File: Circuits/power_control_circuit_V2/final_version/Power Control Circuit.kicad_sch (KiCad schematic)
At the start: 35 parts, among them Q10 IRF1405, Q12 IRF1405, Q23 S8050, Q24 S8550, Q3 S8050, Q4 IRF1405, Q4 S8550, Q8 IRF1405, Q9 IRF1405, U1 PC817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

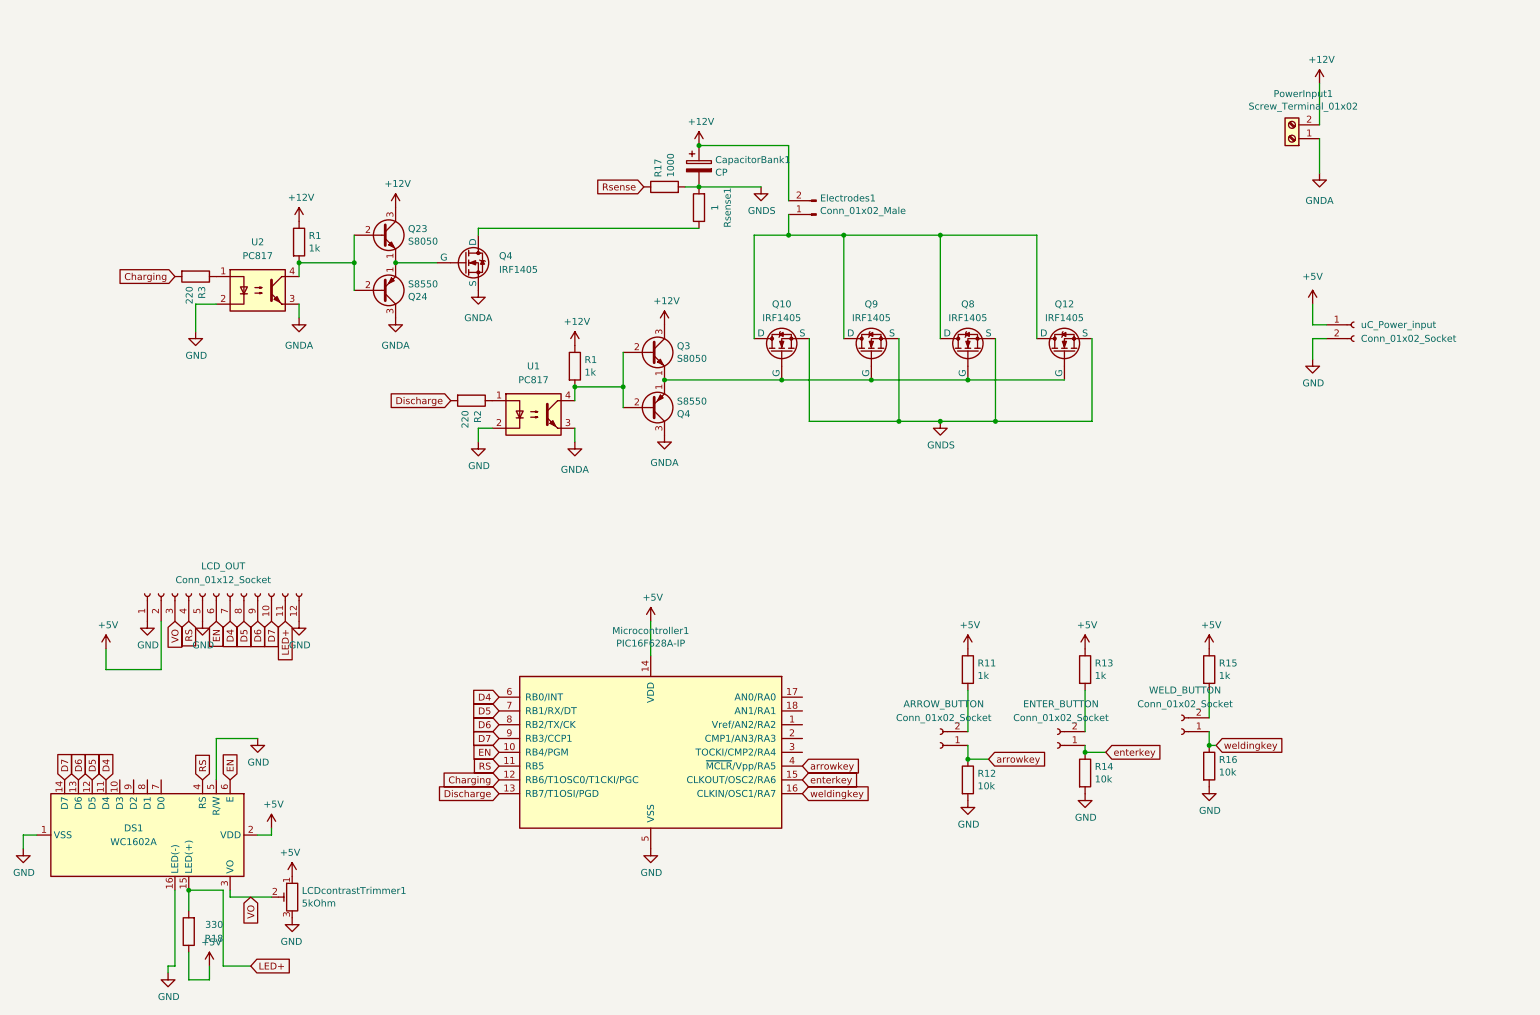
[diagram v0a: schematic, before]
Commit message: finished PCB solution, starting PCB final version|
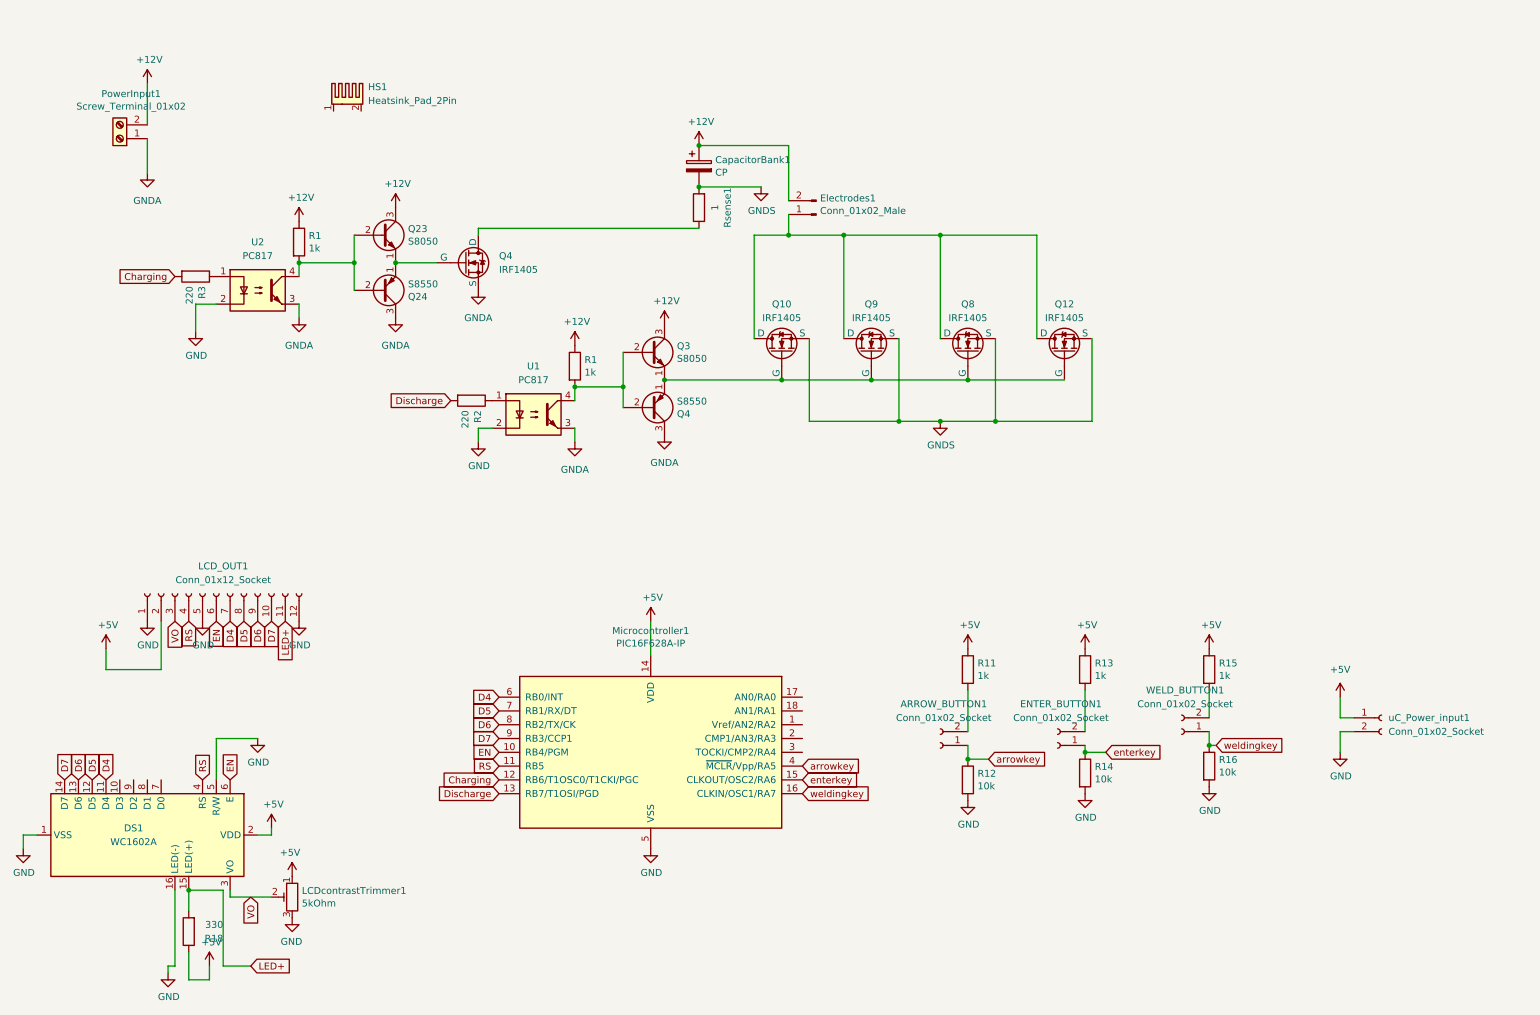
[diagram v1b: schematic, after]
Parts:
- removed R17: 1000, Resistor_THT:R_Axial_DIN0207_L6.3mm_D2.5mm_P7.62mm_Horizontal, symbol Device:R
- added HS1: Heatsink_Pad_2Pin, symbol Mechanical:Heatsink_Pad_2Pin
- ARROW_BUTTON1: renamed from ARROW_BUTTON; footprint (none) -> Connector_JST:JST_EH_B2B-EH-A_1x02_P2.50mm_Vertical
- ENTER_BUTTON1: renamed from ENTER_BUTTON; footprint (none) -> Connector_JST:JST_EH_B2B-EH-A_1x02_P2.50mm_Vertical
- LCDcontrastTrimmer1: footprint trimmer:trimmerEVND8A -> Potentiometer_THT:Potentiometer_Bourns_3386C_Horizontal
- WELD_BUTTON1: renamed from WELD_BUTTON; footprint (none) -> Connector_JST:JST_EH_B2B-EH-A_1x02_P2.50mm_Vertical
- renumbered LCD_OUT to LCD_OUT1, uC_Power_input to uC_Power_input1
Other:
- moved on the sheet: PowerInput1, uC_Power_input1

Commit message: finished PCB final version :)
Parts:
- added HS2, HS3, HS4, HS5: Heatsink_Pad_2Pin, Heatsink:Heatsink_Stonecold_HS-S03_13.21x12.7mm, symbol Mechanical:Heatsink_Pad_2Pin
- HS1: footprint (none) -> Heatsink:Heatsink_Stonecold_HS-S03_13.21x12.7mm
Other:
- moved on the sheet: HS1
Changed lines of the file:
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@@
+    )
+  )
+  (symbol (lib_id "Mechanical:Heatsink_Pad_2Pin") (at 196.85 21.59 0) (unit 1)
+    (in_bom yes) (on_board yes) (dnp no) (fields_autoplaced)
+    (property "Reference" "HS2" (at 200.66 19.685 0)
+      (effects (font (size 1.27 1.27)) (justify left))
+    )
+    (property "Value" "Heatsink_Pad_2Pin" (at 200.66 22.225 0)
+      (effects (font (size 1.27 1.27)) (justify left))
+    )
+    (property "Footprint" "Heatsink:Heatsink_Stonecold_HS-S03_13.21x12.7mm" (at 197.1548 22.86 0)
+      (effects (font (size 1.27 1.27)) hide)
+    )
+    (property "Datasheet" "~" (at 197.1548 22.86 0)
+      (effects (font (size 1.27 1.27)) hide)
+    )
+    (pin "1")
+    (pin "2")
+    (instances
+      (project "Power Control Circuit"
+        (path "/f5e3c383-3430-4217-817e-2eedfeb82870"
+          (reference "HS2") (unit 1)
+        )
+      )
     )
   )
@@
     )
   )
-  (symbol (lib_id "Mechanical:Heatsink_Pad_2Pin") (at 77.47 27.94 0) (unit 1)
-    (in_bom yes) (on_board yes) (dnp no) (fields_autoplaced)
-    (property "Reference" "HS1" (at 81.28 26.035 0)
-      (effects (font (size 1.27 1.27)) (justify left))
-    )
-    (property "Value" "Heatsink_Pad_2Pin" (at 81.28 28.575 0)
-      (effects (font (size 1.27 1.27)) (justify left))
-    )
-    (property "Footprint" "" (at 77.7748 29.21 0)
-      (effects (font (size 1.27 1.27)) hide)
-    )
-    (property "Datasheet" "~" (at 77.7748 29.21 0)
+  (symbol (lib_id "Mechanical:Heatsink_Pad_2Pin") (at 196.85 27.94 0) (unit 1)
+    (in_bom yes) (on_board yes) (dnp no) (fields_autoplaced)
+    (property "Reference" "HS1" (at 200.66 26.035 0)
+      (effects (font (size 1.27 1.27)) (justify left))
+    )
+    (property "Value" "Heatsink_Pad_2Pin" (at 200.66 28.575 0)
+      (effects (font (size 1.27 1.27)) (justify left))
+    )
+    (property "Footprint" "Heatsink:Heatsink_Stonecold_HS-S03_13.21x12.7mm" (at 197.1548 29.21 0)
+      (effects (font (size 1.27 1.27)) hide)
+    )
+    (property "Datasheet" "~" (at 197.1548 29.21 0)
       (effects (font (size 1.27 1.27)) hide)
     )
@@
     )
   )
+  (symbol (lib_id "Mechanical:Heatsink_Pad_2Pin") (at 196.85 15.24 0) (unit 1)
+    (in_bom yes) (on_board yes) (dnp no) (fields_autoplaced)
+    (property "Reference" "HS3" (at 200.66 13.335 0)
+      (effects (font (size 1.27 1.27)) (justify left))
+    )
+    (property "Value" "Heatsink_Pad_2Pin" (at 200.66 15.875 0)
+      (effects (font (size 1.27 1.27)) (justify left))
+    )
+    (property "Footprint" "Heatsink:Heatsink_Stonecold_HS-S03_13.21x12.7mm" (at 197.1548 16.51 0)
+      (effects (font (size 1.27 1.27)) hide)
+    )
+    (property "Datasheet" "~" (at 197.1548 16.51 0)
+      (effects (font (size 1.27 1.27)) hide)
+    )
+    (pin "1")
+    (pin "2")
+    (instances
+      (project "Power Control Circuit"
+        (path "/f5e3c383-3430-4217-817e-2eedfeb82870"
+          (reference "HS3") (unit 1)
+        )
+      )
+    )
+  )
   (symbol (lib_id "power:GND") (at 60.96 146.05 0) (unit 1)
     (in_bom yes) (on_board yes) (dnp no)
@@
         (path "/f5e3c383-3430-4217-817e-2eedfeb82870"
           (reference "#PWR030") (unit 1)
+        )
+      )
+    )
+  )
+  (symbol (lib_id "Mechanical:Heatsink_Pad_2Pin") (at 196.85 34.29 0) (unit 1)
+    (in_bom yes) (on_board yes) (dnp no) (fields_autoplaced)
+    (property "Reference" "HS4" (at 200.66 32.385 0)
+      (effects (font (size 1.27 1.27)) (justify left))
+    )
+    (property "Value" "Heatsink_Pad_2Pin" (at 200.66 34.925 0)
+      (effects (font (size 1.27 1.27)) (justify left))
+    )
+    (property "Footprint" "Heatsink:Heatsink_Stonecold_HS-S03_13.21x12.7mm" (at 197.1548 35.56 0)
+      (effects (font (size 1.27 1.27)) hide)
+    )
+    (property "Datasheet" "~" (at 197.1548 35.56 0)
+      (effects (font (size 1.27 1.27)) hide)
+    )
+    (pin "1")
+    (pin "2")
+    (instances
+      (project "Power Control Circuit"
+        (path "/f5e3c383-3430-4217-817e-2eedfeb82870"
+          (reference "HS4") (unit 1)
         )
       )
@@
         )
       )
+    )
+  )
+  (symbol (lib_id "Mechanical:Heatsink_Pad_2Pin") (at 196.85 40.64 0) (unit 1)
+    (in_bom yes) (on_board yes) (dnp no) (fields_autoplaced)
+    (property "Reference" "HS5" (at 200.66 38.735 0)
+      (effects (font (size 1.27 1.27)) (justify left))
+    )
+    (property "Value" "Heatsink_Pad_2Pin" (at 200.66 41.275 0)
+      (effects (font (size 1.27 1.27)) (justify left))
+    )
+    (property "Footprint" "Heatsink:Heatsink_Stonecold_HS-S03_13.21x12.7mm" (at 197.1548 41.91 0)
+      (effects (font (size 1.27 1.27)) hide)
+    )
+    (property "Datasheet" "~" (at 197.1548 41.91 0)
+      (effects (font (size 1.27 1.27)) hide)
+    )
+    (pin "1")
+    (pin "2")
+    (instances
+      (project "Power Control Circuit"
+        (path "/f5e3c383-3430-4217-817e-2eedfeb82870"
+          (reference "HS5") (unit 1)
+        )
+      )
